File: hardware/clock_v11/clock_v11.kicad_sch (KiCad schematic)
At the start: 227 parts, among them J1 RJ45, J12 Conn_01x03_Pin, J14 DC-005B-2.5A-2.0, J2 Conn_01x03, J4 USB_C_Receptacle, J5 Conn_01x06_Pin, J6 Conn_01x03_Pin, J8 Conn_01x02_Pin, Q1 2N7002, Q10 2N7002, Q9 2N7002, SW1 SW_Push_4PDT, U1 ADA4807-1, U10 STM32F405RGTx, U11 AMS1117-3.3, U12 BA50DD0WHFP-TR, U13 M24C02-RMN, U14 CH340C, U15 USBLC6-2P6, U16 TLV3603DCKR, U17 SN74LVC1G14DBV, U18 TMP112AIDRLR, U19 SN74LVC1G14DBV, U2 SN74LVC1G14DBV, U20 SN74LVC1G14DBV, U21 SN74LVC1G14DBV, U23 TPS63060, U3 SN74LVC1G14DBV, U4 ADA4807-1, U5 ADA4807-1, U6 TLV3603DCKR, U7 SN74LVC1G14DBV, U8 TLV3603DCKR, U9 L78L05_SOT89, Y1 AOCJY4A-10.000MHZ-SW, Y2 16MHz

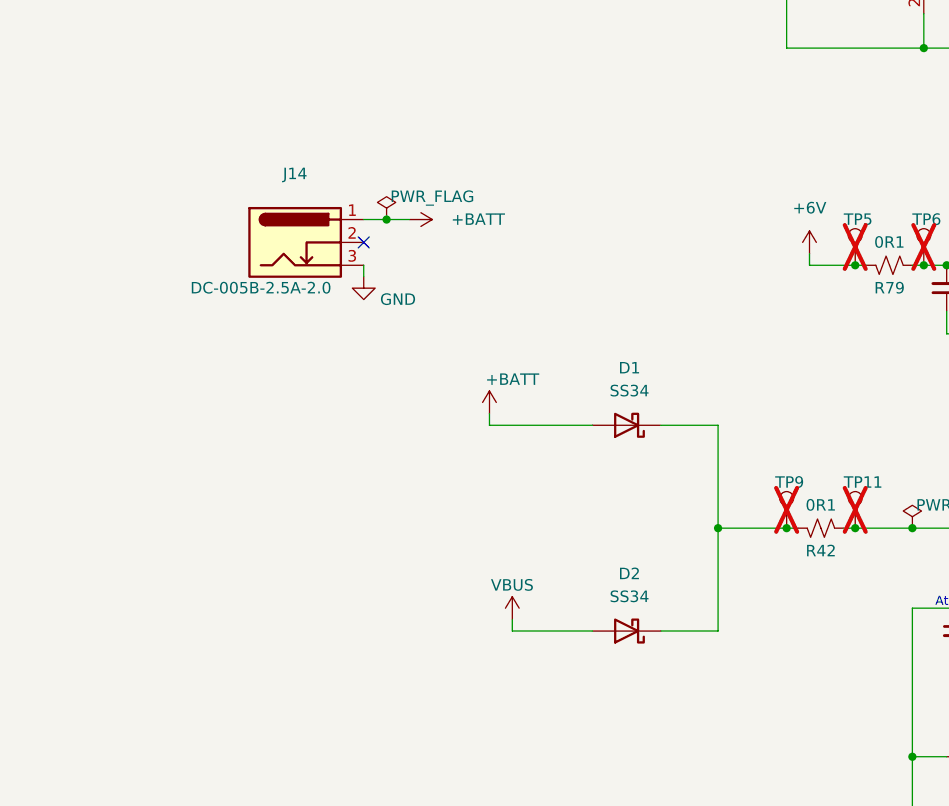
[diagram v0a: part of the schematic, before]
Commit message: make clock board USB power only. Fixes #307
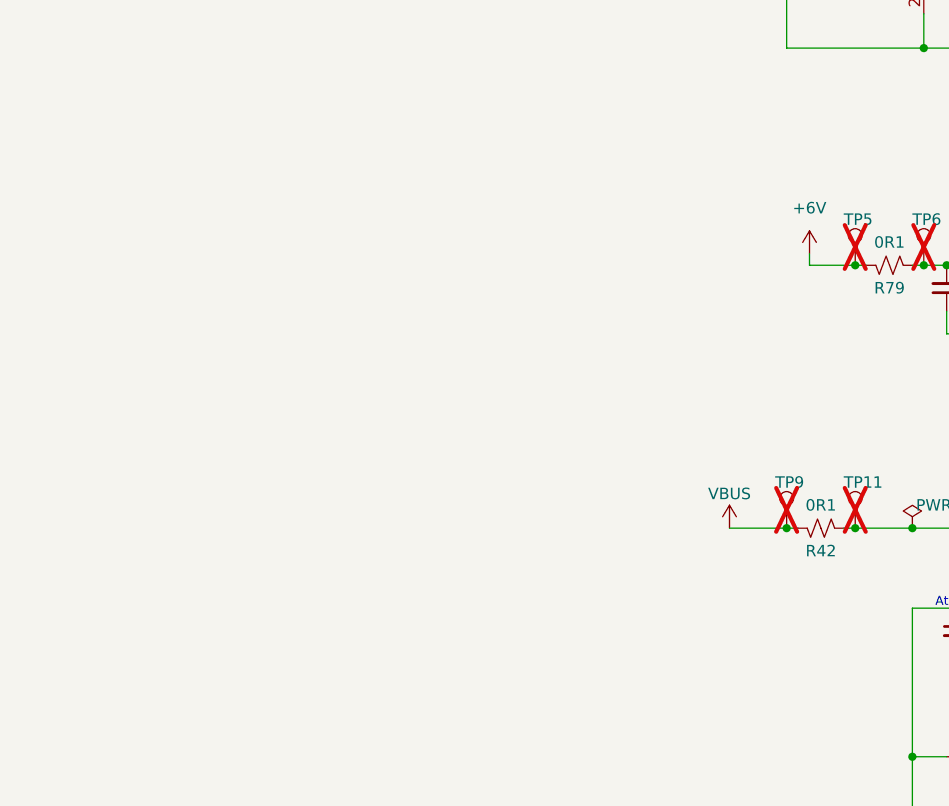
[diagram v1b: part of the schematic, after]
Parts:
- removed D1, D2: SS34, Diode_SMD:D_SMA, symbol Diode:MBRA340
- removed J14: DC-005B-2.5A-2.0, Connector_BarrelJack:BarrelJack_Horizontal, symbol Connector:Barrel_Jack_Switch_Pin3Ring
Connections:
- net VBUS: now also R42.2, TP9.1
- no-connect marks 39 -> 38

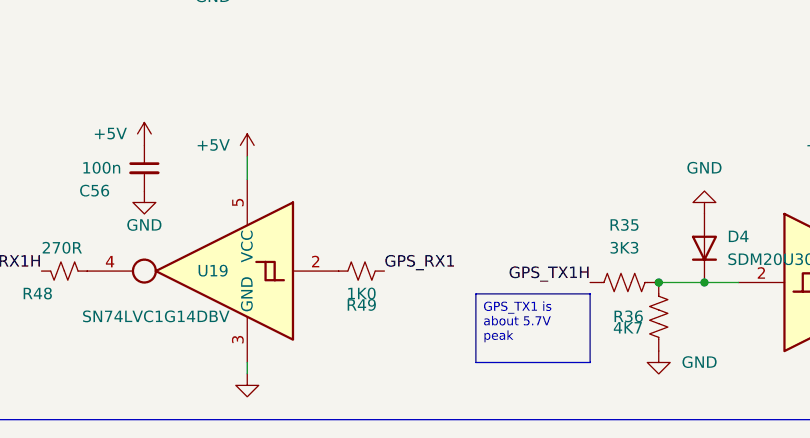
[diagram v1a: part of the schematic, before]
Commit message: Remove R49. Fixes #303
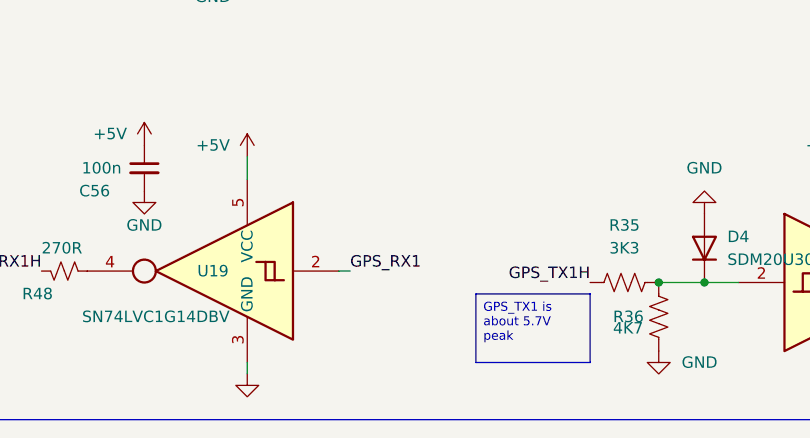
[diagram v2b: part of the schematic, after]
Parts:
- removed R49: 1K0, Resistor_SMD:R_0603_1608Metric, symbol Device:R_Small_US
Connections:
- net GPS_RX1: now also U19.2
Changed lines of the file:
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@@
     (stroke (width 0) (type default))
   )
+  (wire (pts (xy 336.55 397.51) (xy 337.82 397.51))
+    (stroke (width 0) (type default))
+  )
   (wire (pts (xy 95.25 30.48) (xy 95.25 27.94))
     (stroke (width 0) (type default))
@@
     (effects (font (size 1.27 1.27)) (justify left bottom))
   )
-  (label "GPS_RX1" (at 341.63 397.51 0) (fields_autoplaced)
+  (label "GPS_RX1" (at 337.82 397.51 0) (fields_autoplaced)
     (effects (font (size 1.27 1.27)) (justify left bottom))
   )
@@
         )
       )
-    )
-  )
-  (symbol (lib_id "Device:R_Small_US") (at 339.09 397.51 270) (unit 1)
-    (in_bom yes) (on_board yes) (dnp no)
-    (property "Reference" "R49" (at 339.09 401.32 90)
-      (effects (font (size 1.27 1.27)))
-    )
-    (property "Value" "1K0" (at 339.09 400.05 90)
-      (effects (font (size 1.27 1.27)))
-    )
-    (property "Footprint" "Resistor_SMD:R_0603_1608Metric" (at 339.09 397.51 0)
-      (effects (font (size 1.27 1.27)) hide)
-    )
-    (property "Datasheet" "~" (at 339.09 397.51 0)
-      (effects (font (size 1.27 1.27)) hide)
-    )
-    (property "LCSC" "" (at 339.09 397.51 0)
-      (effects (font (size 1.27 1.27)) hide)
-    )
-    (property "JLCPCB Part #" "C21190" (at 339.09 397.51 0)
-      (effects (font (size 1.27 1.27)) hide)
-    )
-    (pin "1")
-    (pin "2")
-    (instances
-      (project "clock_v11"
-        (path "/bd4d3b9a-07c1-4a53-9c94-2893f3e869d4"
-          (reference "R49") (unit 1)
-        )
-      )

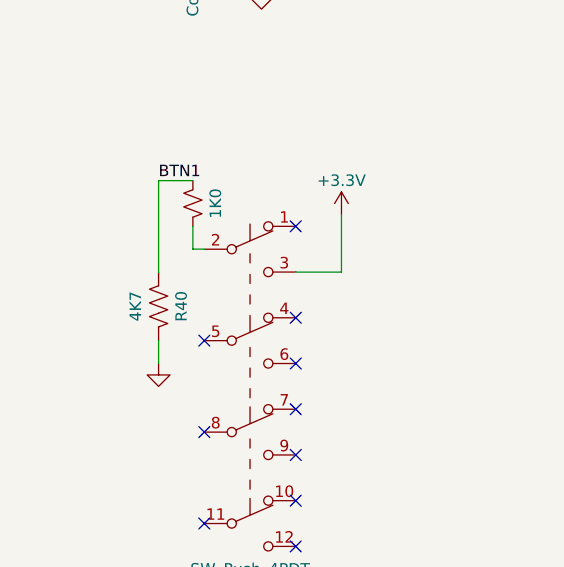
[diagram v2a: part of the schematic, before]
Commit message: remove needless pull down reistors. Fixes #304
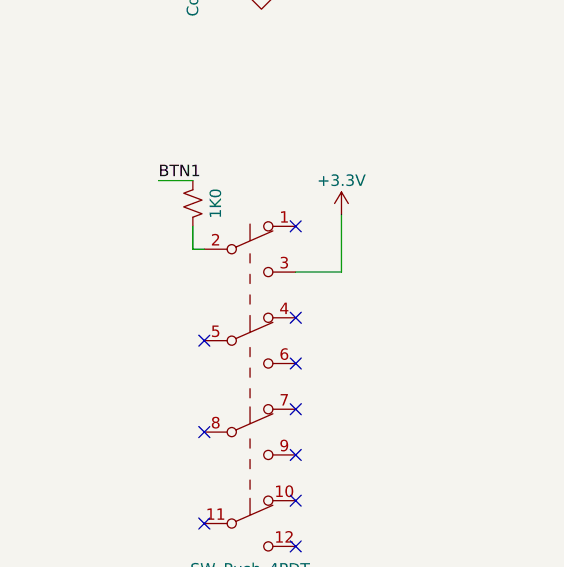
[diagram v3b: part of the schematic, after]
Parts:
- removed R40: 4K7, Resistor_SMD:R_0603_1608Metric, symbol Device:R_US
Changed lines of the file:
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@@
     (stroke (width 0) (type default))
   )
-  (wire (pts (xy 38.1 179.07) (xy 38.1 168.91))
-    (stroke (width 0) (type default))
-  )
   (wire (pts (xy 379.73 187.96) (xy 381 187.96))
     (stroke (width 0) (type default))
@@
     (stroke (width 0) (type default))
   )
-  (wire (pts (xy 38.1 168.91) (xy 41.91 168.91))
-    (stroke (width 0) (type default))
-  )
   (wire (pts (xy 327.66 193.04) (xy 327.66 187.96))
     (stroke (width 0) (type default))
@@
     (stroke (width 0) (type default))
   )
-  (wire (pts (xy 38.1 186.69) (xy 38.1 189.23))
-    (stroke (width 0) (type default))
-  )
   (wire (pts (xy 367.03 31.75) (xy 364.49 31.75))
     (stroke (width 0) (type default))
@@
     (stroke (width 0) (type default))
   )
+  (wire (pts (xy 38.1 168.91) (xy 41.91 168.91))
+    (stroke (width 0) (type default))
+  )
   (wire (pts (xy 182.88 387.35) (xy 190.5 387.35))
     (stroke (width 0) (type default))
@@
     )
   )
-  (symbol (lib_id "power:GND") (at 38.1 189.23 0) (mirror y) (unit 1)
-    (in_bom yes) (on_board yes) (dnp no)
-    (property "Reference" "#PWR090" (at 38.1 195.58 0)
-      (effects (font (size 1.27 1.27)) hide)
-    )
-    (property "Value" "GND" (at 35.56 191.77 0)
-      (effects (font (size 1.27 1.27)) hide)
-    )
-    (property "Footprint" "" (at 38.1 189.23 0)
-      (effects (font (size 1.27 1.27)) hide)
-    )
-    (property "Datasheet" "" (at 38.1 189.23 0)
-      (effects (font (size 1.27 1.27)) hide)
-    )
-    (pin "1")
-    (instances
-      (project "clock_v11"
-        (path "/bd4d3b9a-07c1-4a53-9c94-2893f3e869d4"
-          (reference "#PWR090") (unit 1)
-        )
-      )
-    )
-  )
   (symbol (lib_id "power:+5VA") (at 295.91 72.39 0) (unit 1)
     (in_bom yes) (on_board yes) (dnp no)
@@
         )
       )
-    )
-  )
-  (symbol (lib_id "Device:R_US") (at 38.1 182.88 0) (mirror x) (unit 1)
-    (in_bom yes) (on_board yes) (dnp no)
-    (property "Reference" "R40" (at 40.64 182.88 90)
-      (effects (font (size 1.27 1.27)))
-    )
-    (property "Value" "4K7" (at 35.56 182.88 90)
-      (effects (font (size 1.27 1.27)))
-    )
-    (property "Footprint" "Resistor_SMD:R_0603_1608Metric" (at 39.116 182.626 90)
-      (effects (font (size 1.27 1.27)) hide)
-    )
-    (property "Datasheet" "~" (at 38.1 182.88 0)
-      (effects (font (size 1.27 1.27)) hide)
-    )
-    (property "LCSC" "" (at 38.1 182.88 0)
-      (effects (font (size 1.27 1.27)) hide)
-    )
-    (property "JLCPCB Part #" "C23162" (at 38.1 182.88 0)
-      (effects (font (size 1.27 1.27)) hide)
-    )
-    (pin "1")
-    (pin "2")
-    (instances
-      (project "clock_v11"
-        (path "/bd4d3b9a-07c1-4a53-9c94-2893f3e869d4"
-          (reference "R40") (unit 1)
-        )
-      )

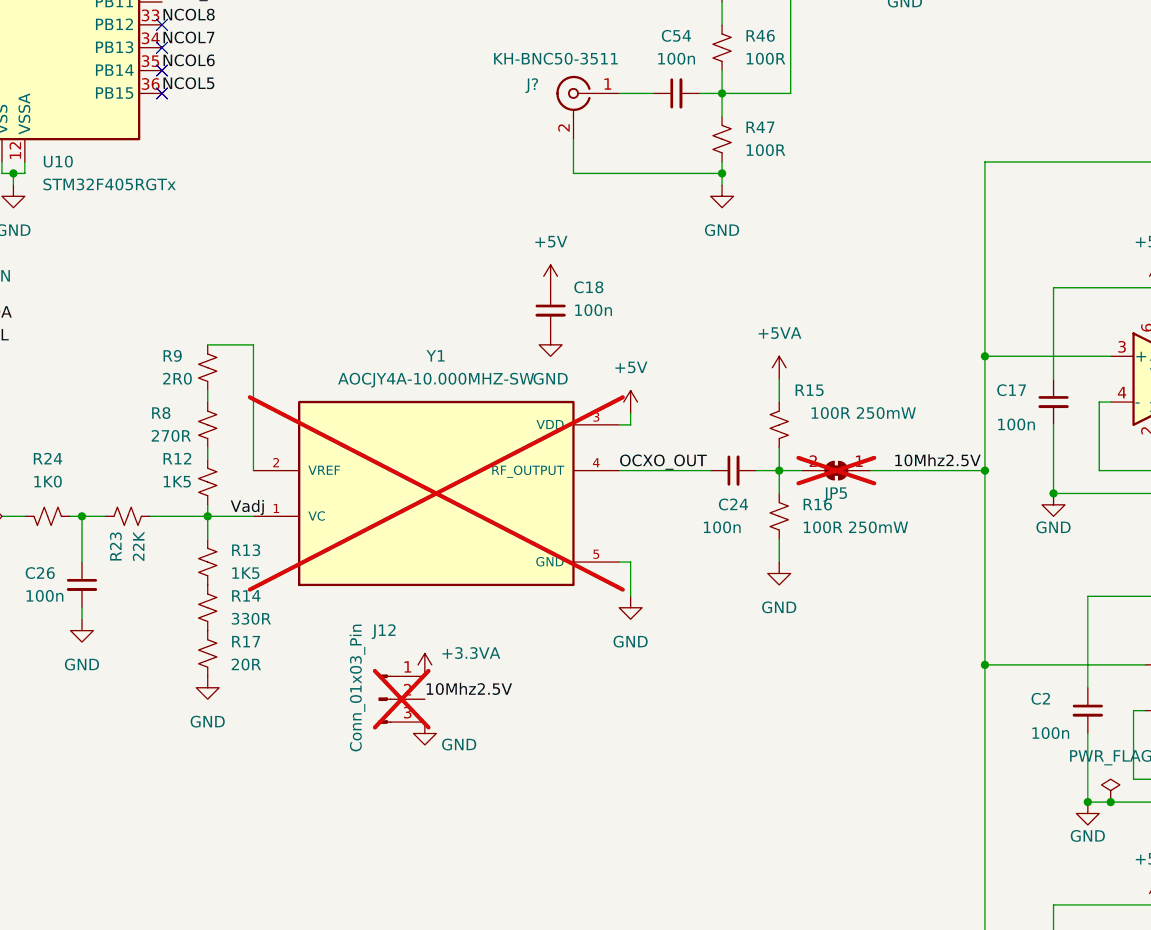
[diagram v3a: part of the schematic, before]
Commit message: update with sockets for differnt oscilators
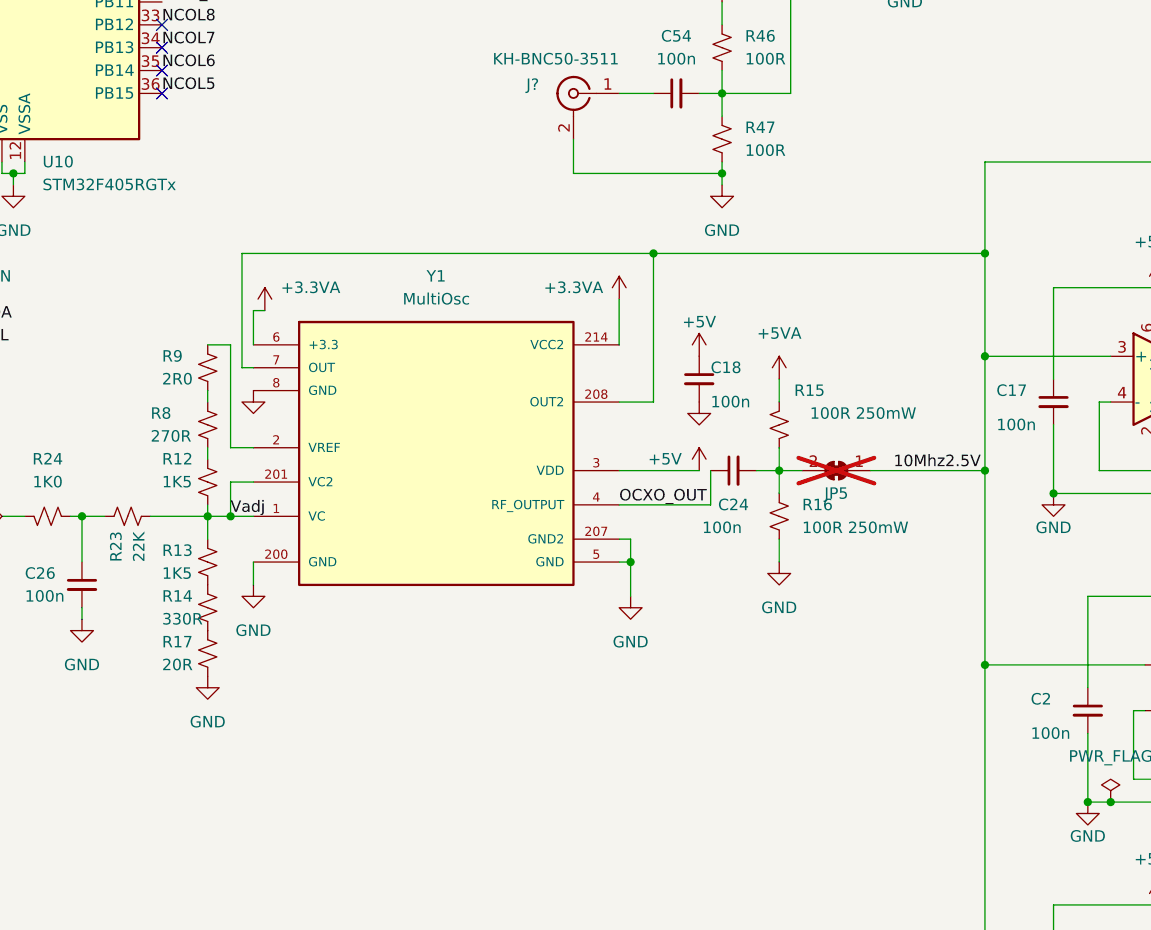
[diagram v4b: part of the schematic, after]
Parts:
- removed J12: Conn_01x03_Pin, Connector_PinHeader_2.54mm:PinHeader_1x03_P2.54mm_Vertical, symbol Connector:Conn_01x03_Pin
- removed Y1: AOCJY4A-10.000MHZ-SW, blinky_footprints:XTAL_AOCJY4A-10.000MHZ-SW, symbol BlinkyShared:AOCJY4A-10.000MHZ-SW
- added Y1: MultiOsc, blinky_footprints:XTAL_Multi, symbol BlinkyShared:OSC_Multi
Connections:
- net +3.3VA: now also Y1.214 (VCC2), Y1.6 (+3.3)
- net +5V: now also Y1.3 (VDD)
- net 10Mhz2.5V: now also Y1.208 (OUT2), Y1.7 (OUT)
- net GND: now also Y1.200 (GND), Y1.207 (GND2), Y1.5 (GND), Y1.8 (GND)
- net OCXO_OUT: now also Y1.4 (RF_OUTPUT)
- net Vadj: now also Y1.1 (VC), Y1.201 (VC2)
- net at R9.1: now also Y1.2 (VREF)
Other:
- moved on the sheet: C18

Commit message: chance current sense resistor. Fixes#308
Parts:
- R42: value 0R1 -> 0R020; JLCPCB Part # C25334 -> C2765435
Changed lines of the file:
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@@
       (effects (font (size 1.27 1.27)))
     )
-    (property "Value" "0R1" (at 120.65 360.68 90)
+    (property "Value" "0R020" (at 120.65 360.68 90)
       (effects (font (size 1.27 1.27)))
     )
@@
       (effects (font (size 1.27 1.27)) hide)
     )
-    (property "JLCPCB Part #" "C25334" (at 120.65 363.22 0)
+    (property "JLCPCB Part #" "C2765435" (at 120.65 363.22 0)
       (effects (font (size 1.27 1.27)) hide)
     )

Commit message: fix up footprints
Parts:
- U23: footprint Package_SON:Texas_S-PWSON-N10_ThermalVias -> blinky_footprints:Texas_S-PWSON-N10_ThermalVias-CJ
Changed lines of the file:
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@@
       (effects (font (size 1.27 1.27)))
     )
-    (property "Footprint" "Package_SON:Texas_S-PWSON-N10_ThermalVias" (at 172.72 398.78 0)
+    (property "Footprint" "blinky_footprints:Texas_S-PWSON-N10_ThermalVias-CJ" (at 172.72 398.78 0)
       (effects (font (size 1.27 1.27)) hide)
     )

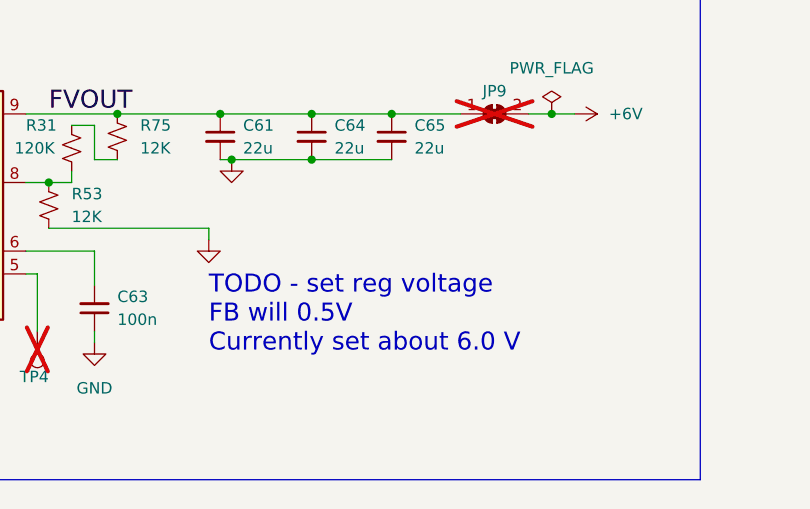
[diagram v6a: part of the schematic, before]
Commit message: update blink from 6V to 4.7V
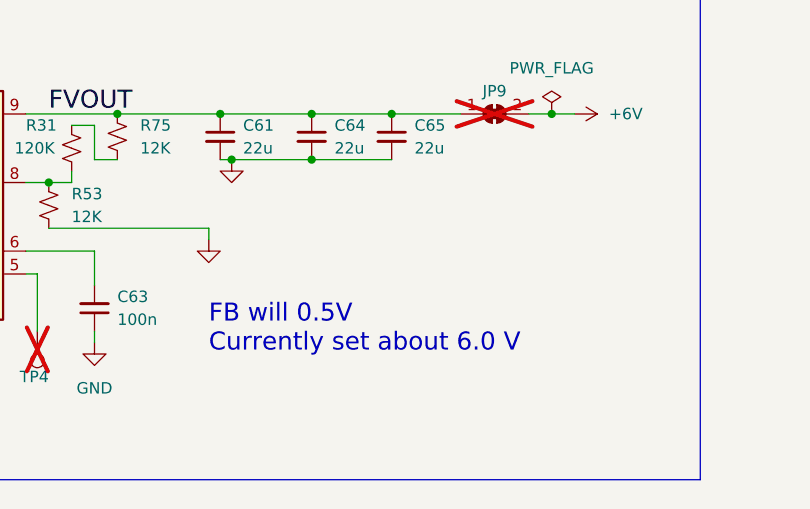
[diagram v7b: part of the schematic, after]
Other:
- note added: "FB will 0.5V Currently set about 6.0 V"
- note removed: "TODO - set reg voltage FB will 0.5V Currently set about 6.0 V"
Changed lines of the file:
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@@
     (effects (font (size 1.27 1.27)) (justify left bottom))
   )
-  (text "TODO - set reg voltage\nFB will 0.5V \nCurrently set about 6.0 V "
-    (at 203.2 398.78 0)
+  (text "FB will 0.5V \nCurrently set about 6.0 V " (at 203.2 398.78 0)
     (effects (font (size 2 2)) (justify left bottom))
   )
